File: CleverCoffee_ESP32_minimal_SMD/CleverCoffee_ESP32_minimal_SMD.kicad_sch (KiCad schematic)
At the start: 25 parts

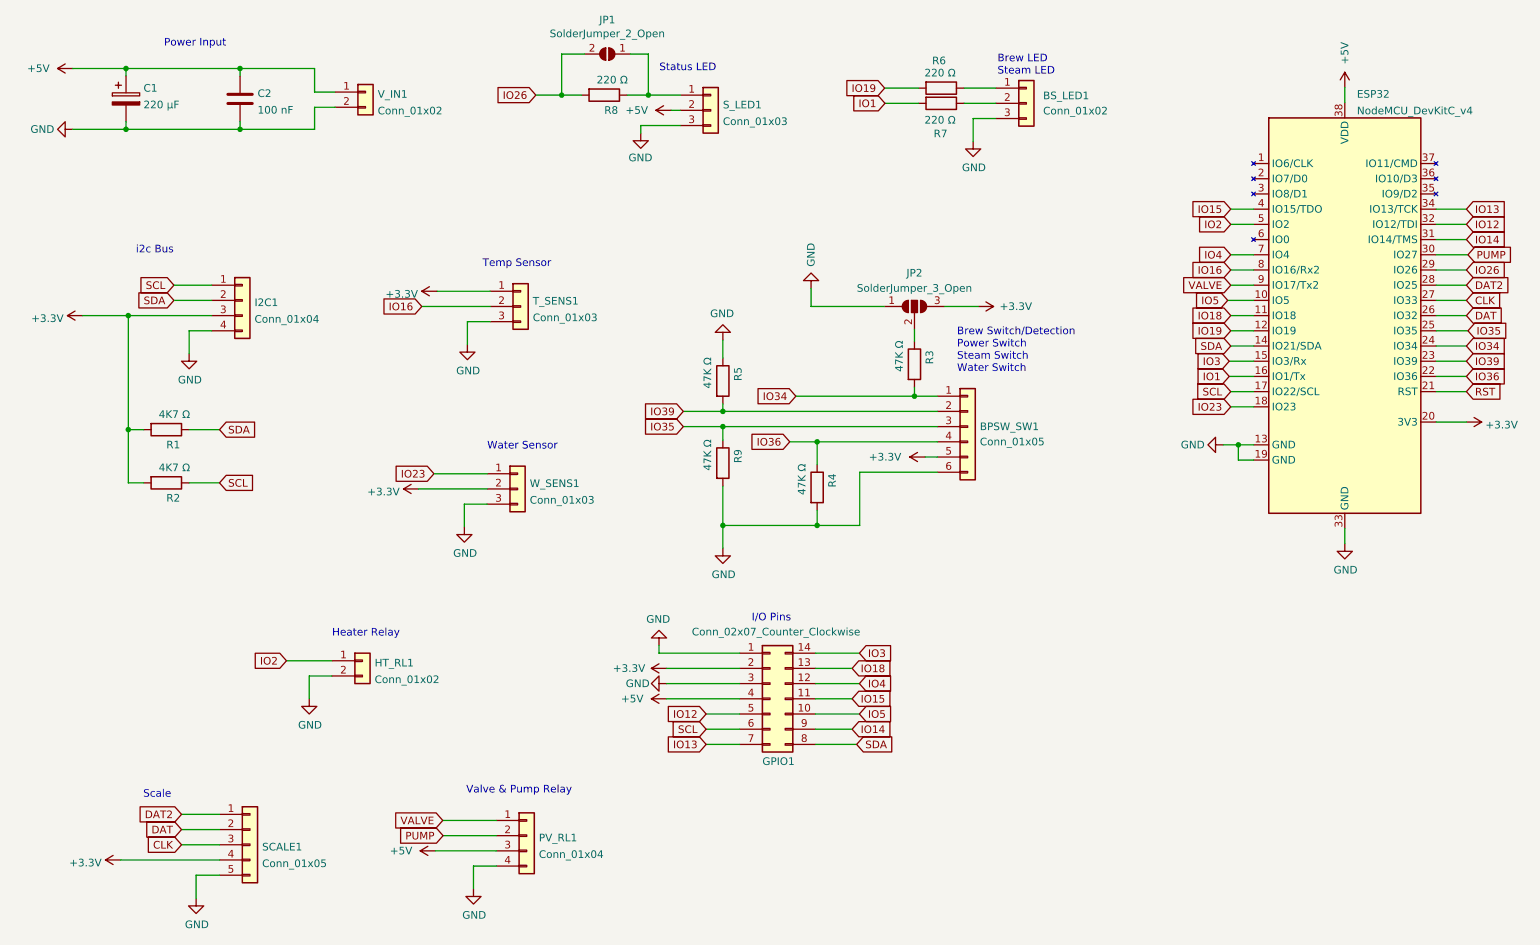
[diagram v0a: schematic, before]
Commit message: Update ESP32 minimal SMD with features from minimal v1.6
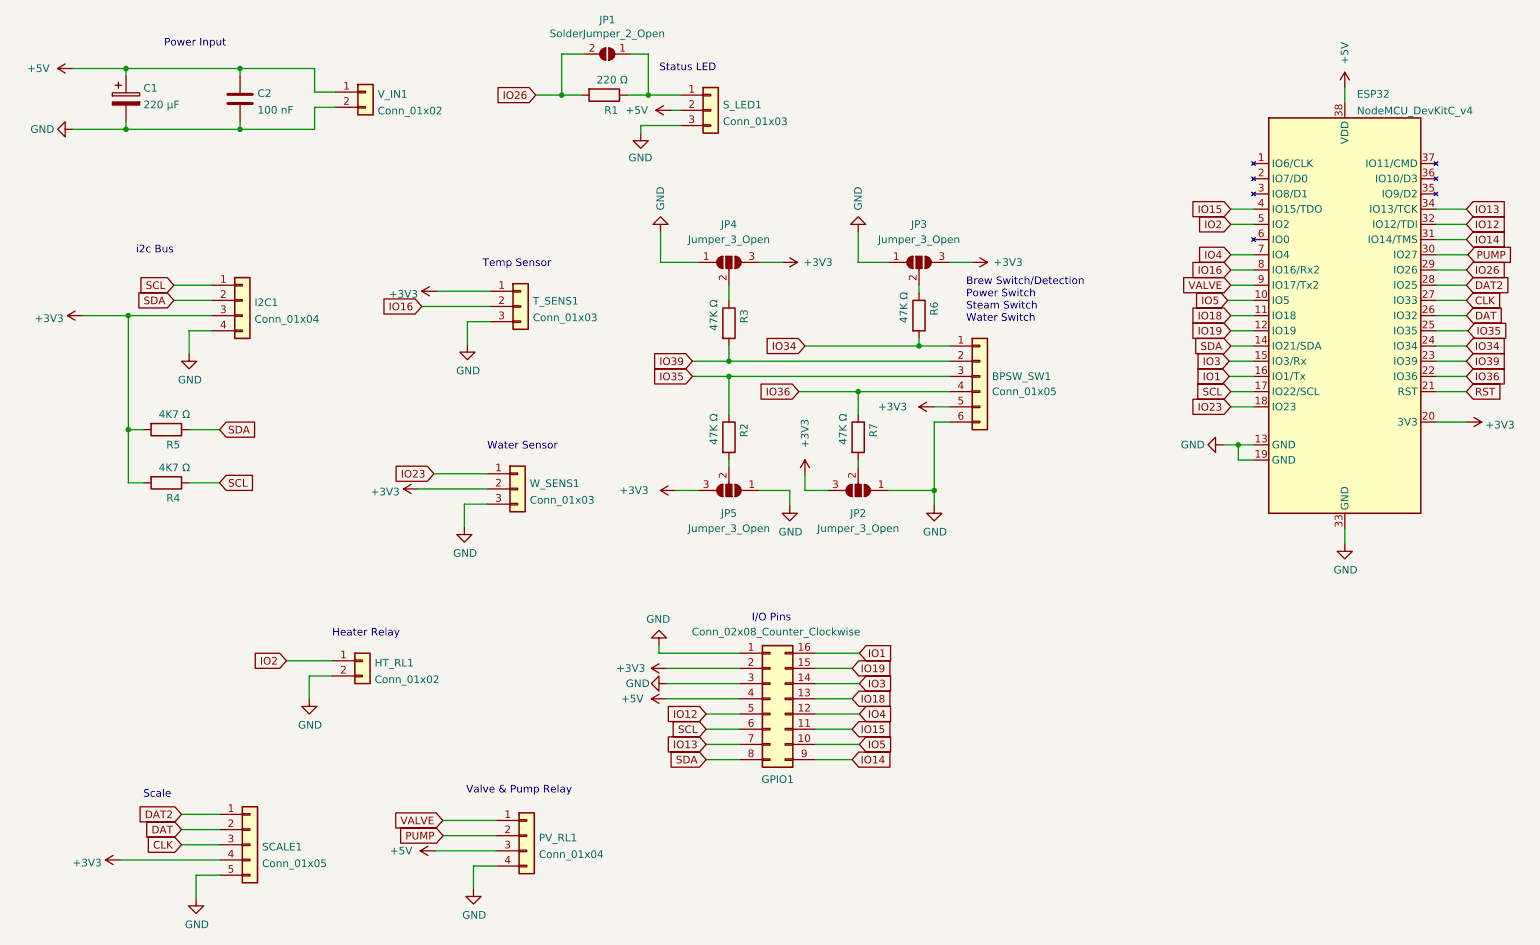
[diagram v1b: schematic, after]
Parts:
- removed BS_LED1: Conn_01x02, Connector_PinSocket_2.54mm:PinSocket_1x03_P2.54mm_Vertical, symbol Connector_Generic:Conn_01x03
- removed R6, R7: 220 Ω, Resistor_SMD:R_1206_3216Metric_Pad1.30x1.75mm_HandSolder, symbol Device:R
- added JP3, JP4, JP5: Jumper_3_Open, Jumper:SolderJumper-3_P1.3mm_Open_Pad1.0x1.5mm, symbol Jumper:SolderJumper_3_Open
- GPIO1: value Conn_02x07_Counter_Clockwise -> Conn_02x08_Counter_Clockwise; footprint Connector_PinSocket_2.54mm:PinSocket_2x07_P2.54mm_Vertical -> Connector_PinSocket_2.54mm:PinSocket_2x08_P2.54mm_Vertical; symbol Connector_Generic:Conn_02x07_Counter_Clockwise -> Connector_Generic:Conn_02x08_Counter_Clockwise
- JP2: value SolderJumper_3_Open -> Jumper_3_Open; now left out of the parts list
- renumbered R8 to R1, R9 to R2, R5 to R3, R2 to R4, R1 to R5, R3 to R6, R4 to R7
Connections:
- net +3V3: now also JP3.3 (B), JP4.3 (B), JP5.3 (B)
- net GND: now also JP3.1 (A), JP4.1 (A), JP5.1 (A); no longer R2.2, R3.1, R7.2
- net IO1: now also GPIO1.16 (Pin_16)
- net IO19: now also GPIO1.15 (Pin_15)
- net at JP2.2 (C): now also R7.2; no longer R6.1
- new net: JP5.2 (C), R2.2
- new net: JP4.2 (C), R3.1
- new net: JP3.2 (C), R6.1
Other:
- note removed: "Brew LED Steam LED"
- title: ESP32 Breakout Board - SMD -> ESP32 Breakout Board - Minimal SMD
- moved on the sheet: BPSW_SW1, R2, R3, R6, R7

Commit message: change solder jumper to bridged gnd
solderjumper für switch inputs are now bridged to gnd
changed Revision to 1.2
add local KidCad history to gitignore
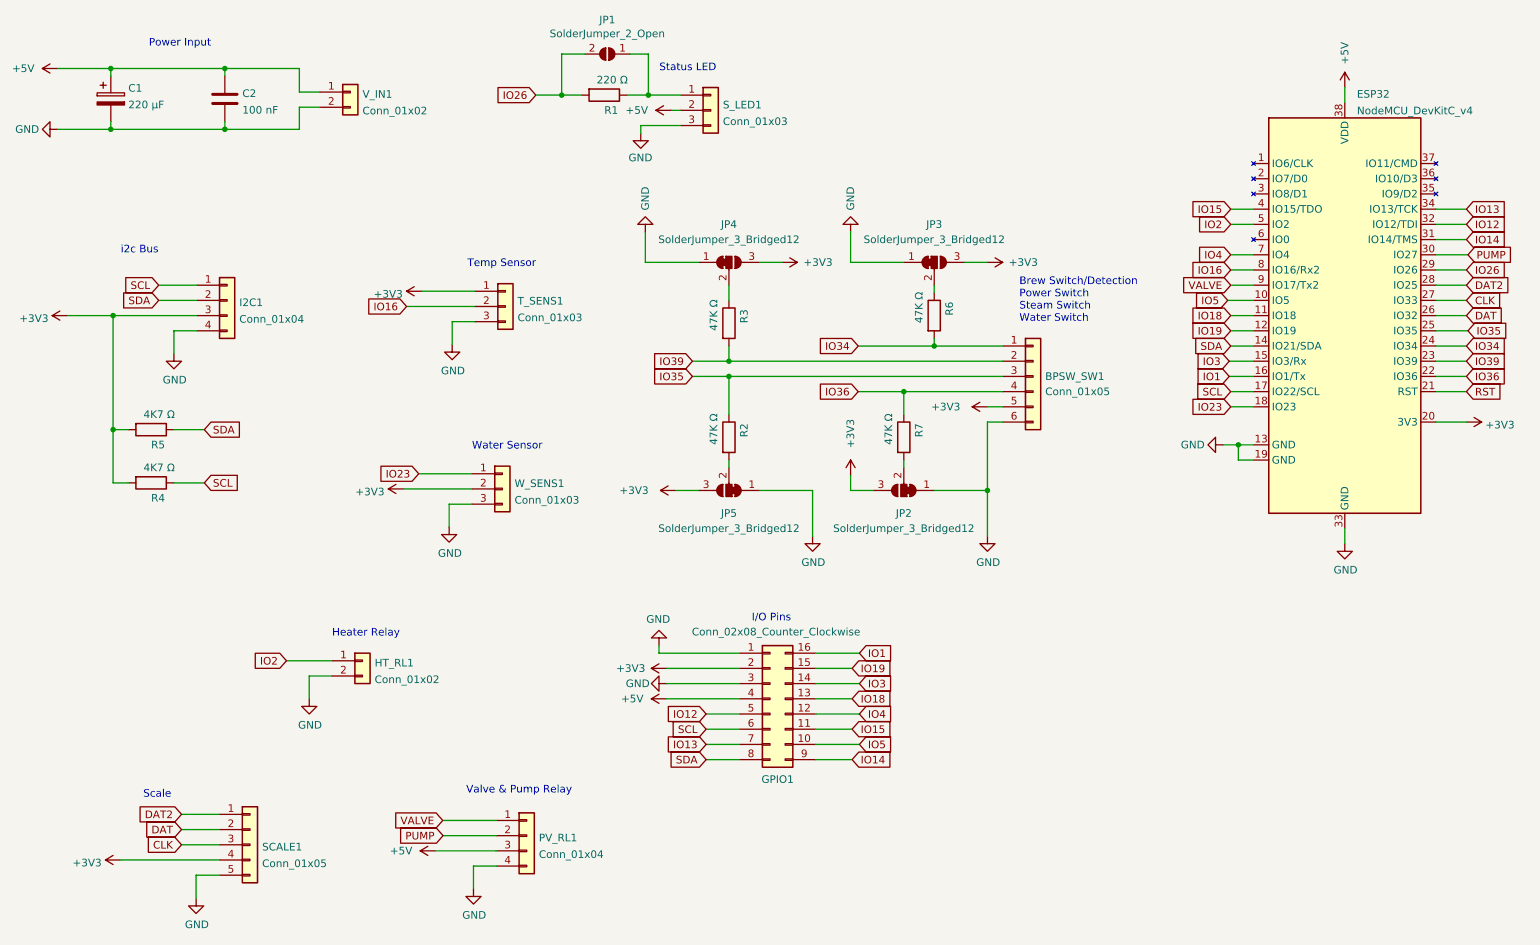
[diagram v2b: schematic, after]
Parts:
- JP2, JP3, JP4, JP5: value Jumper_3_Open -> SolderJumper_3_Bridged12; footprint Jumper:SolderJumper-3_P1.3mm_Open_Pad1.0x1.5mm -> Jumper:SolderJumper-3_P1.3mm_Bridged12_Pad1.0x1.5mm; symbol Jumper:SolderJumper_3_Open -> Jumper:SolderJumper_3_Bridged12
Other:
- moved on the sheet: BPSW_SW1, C1, C2, I2C1, R4, R5, R6, R7, T_SENS1, V_IN1, W_SENS1
